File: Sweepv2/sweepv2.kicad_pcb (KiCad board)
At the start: 2 copper layers, 217.3 x 86.9 mm, 49 parts, among them J1 AudioJack4dpb, J2 AudioJack4dpb, SW10 SW_Push, SW11 SW_Push, SW11_r1 SW_Push, SW12 SW_Push, SW12_r1 SW_Push, SW13_r1 SW_Push, SW14 SW_Push, SW15 SW_Push, SW15_r1 SW_Push, SW16 SW_Push, SW16_r1 SW_Push, SW17 SW_Push, SW17_r1 SW_Push, SW18 SW_Push, SW18_r1 SW_Push, SW2 SW_Push, SW20 SW_Push, SW20_r1 SW_Push, SW21 SW_Push, SW21_r1 SW_Push, SW2_r1 SW_Push, SW3 SW_Push, SW3_r1 SW_Push, SW4 SW_Push, SW4_r1 SW_Push, SW5 SW_Push, SW5_r1 SW_Push, SW6 SW_Push, SW6_r1 SW_Push, SW7_r1 SW_Push, SW8 SW_Push, SW8_r1 SW_Push, SW9 SW_Push, SW9_r1 SW_Push, U1 ProMicro-kbd, U2 ProMicro-kbd

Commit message: bom comment changes
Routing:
- net Switch16_r: track 63.1 -> 66.0 mm
- net Switch11_r: track 97.7 -> 99.9 mm
- net Switch11: track 135.0 -> 136.4 mm
- net Switch17: track 45.5 -> 46.4 mm

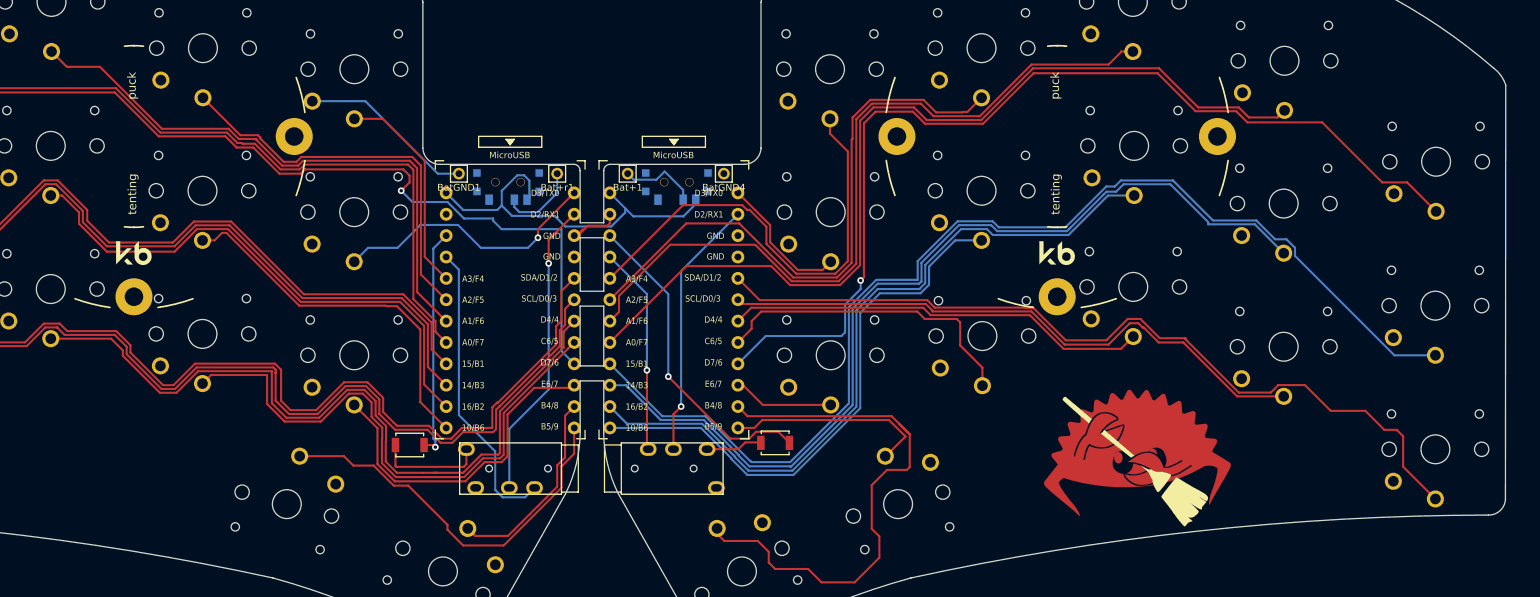
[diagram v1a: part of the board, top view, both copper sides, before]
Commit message: better switch placement but still actually all over, don't use.
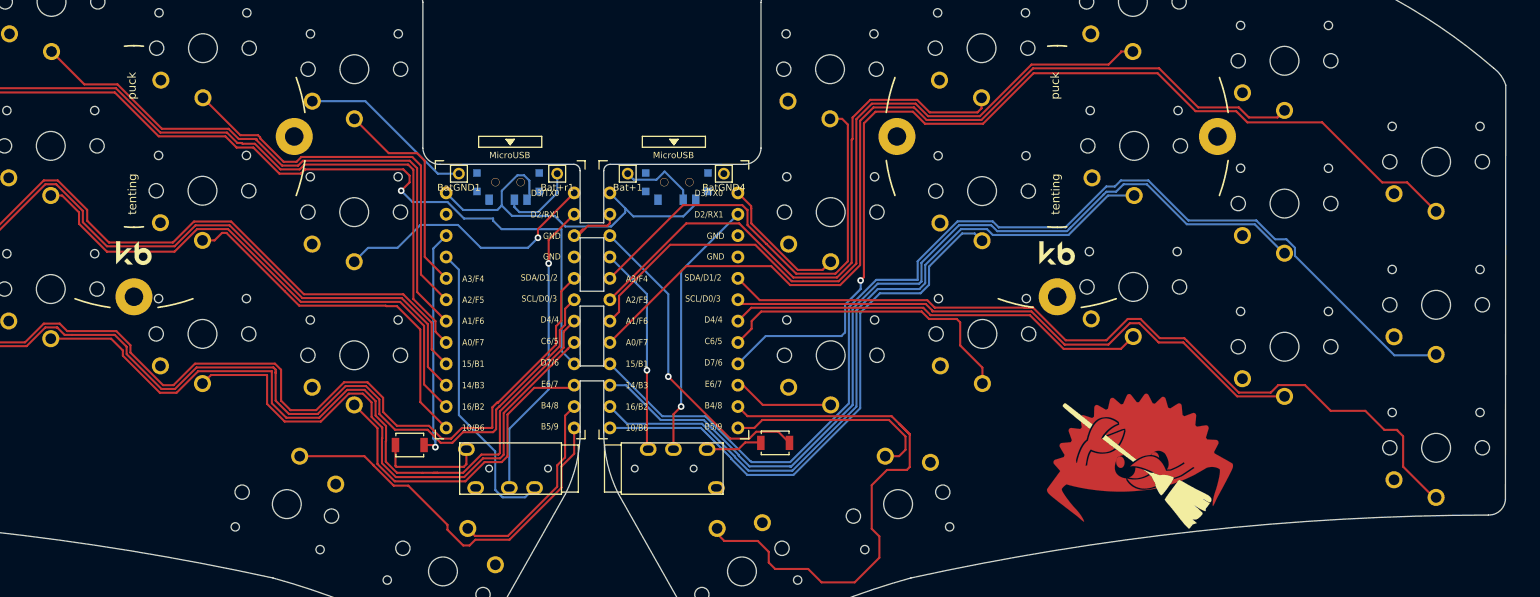
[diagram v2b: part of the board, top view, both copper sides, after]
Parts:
- moved G*** 0.57 mm to (185.9, 77.0), turned to 7 degrees
- moved SW16_r1 0.25 mm to (168.7, 61.5)
- moved SW13_r1 0.20 mm to (222.6, 75.0)
- moved SW7_r1 0.13 mm to (222.6, 58.0)
- moved SW18_r1 0.10 mm to (204.6, 63.0)
- moved SW8_r1 0.10 mm to (204.6, 46.0)
- moved SW11_r1 0.07 mm to (168.6, 44.5)
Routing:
- net Switch17_r: track 24.5 -> 25.4 mm
- net Switch4_r: track 70.7 -> 71.5 mm
- net Switch5_r: track 54.9 -> 55.6 mm
- net Switch9_r: track 66.0 -> 66.7 mm

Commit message: better alignment?
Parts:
- moved SW15_r1 0.26 mm to (186.5, 56.1)
- moved SW9_r1 0.15 mm to (186.5, 39.1)
- moved SW16_r1 0.10 mm to (168.6, 61.5)
- moved SW10 0.09 mm to (58.0, 39.1)
- moved SW16 0.09 mm to (58.0, 56.1)
- moved SW12_r1 0.08 mm to (150.5, 47.0)
- moved SW17_r1 0.08 mm to (150.5, 64.0)
- moved SW11_r1 0.07 mm to (168.6, 44.5)
- moved SW11 0.05 mm to (76.0, 44.5)
- moved SW17 0.05 mm to (76.0, 61.5)
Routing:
- net Switch6_r: track 134.6 -> 135.2 mm
